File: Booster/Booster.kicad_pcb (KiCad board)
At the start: 2 copper layers, 97 x 60 mm, 120 parts, among them IC401 SN754410, J101 Track, J301 15VDC, J601 StatusLED, J701 Conn_01x04, P201 CONN_01X02, P202 CONN_01X02, P601 ~OVERCURRENT_OUT, P602 ~OVERCURRENT_OUT_OP, P603 MSTR_SW, P604 MSTR_SW_OUT, P605 MSTR_SW_OUT_OP, P606 ~DRIVER_ENABLE_OUT_OP, P607 ~DRIVER_ENABLE_OUT, P701 REVERSER_OUT, P702 REVERSER_OUT_OP, Q601 BC807-40, Q602 BC807-40, Q603 BC807-40, Q604 BC817-40, Q701 BC817-40, SW601 DIP, U201 6N137, U203 LM339, U301 LM7805_TO220, U501 LM338, U502 LM358, U503 NE555, U504 74HC08, U602 PC817, U603 PC817, U604 PC817, U701 74HC86, U702 PC817

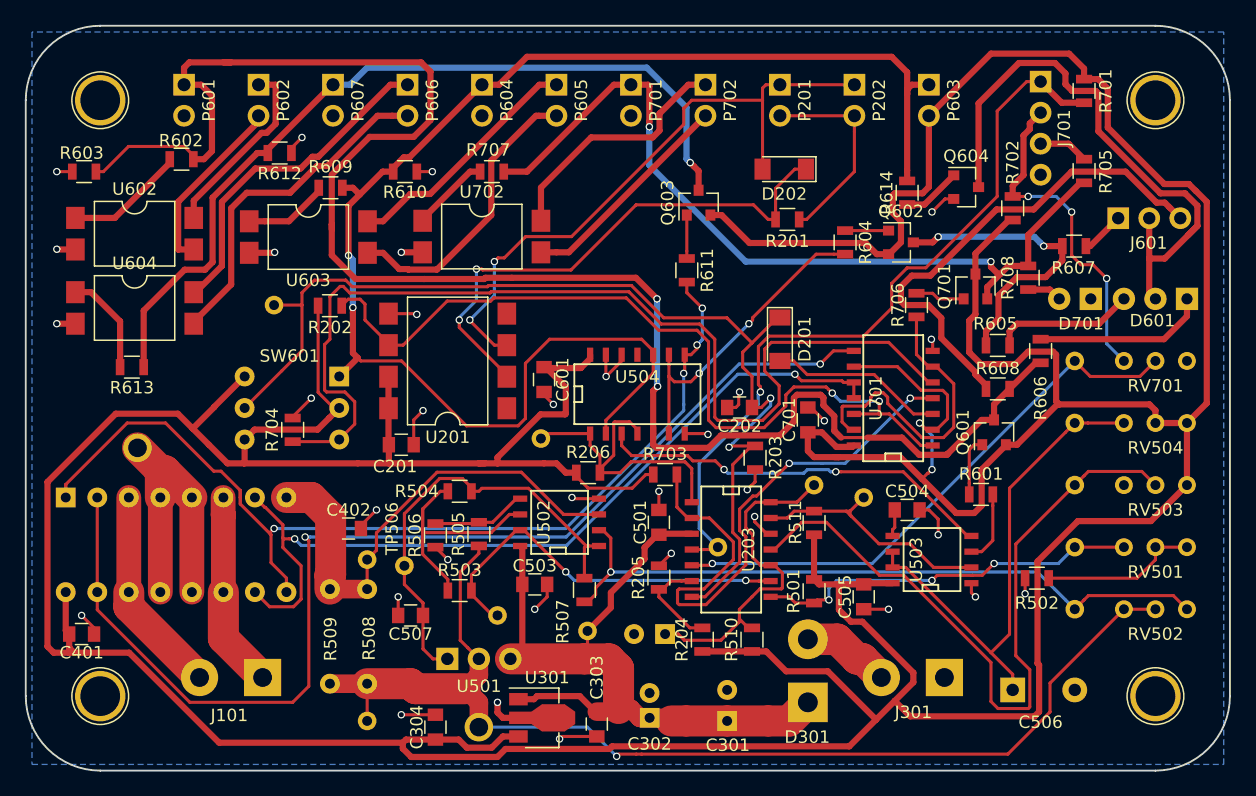
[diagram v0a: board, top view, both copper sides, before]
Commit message: Fixed track clearance (one DRC validation fail as well as a few tracks unnecessary close to through whole components.
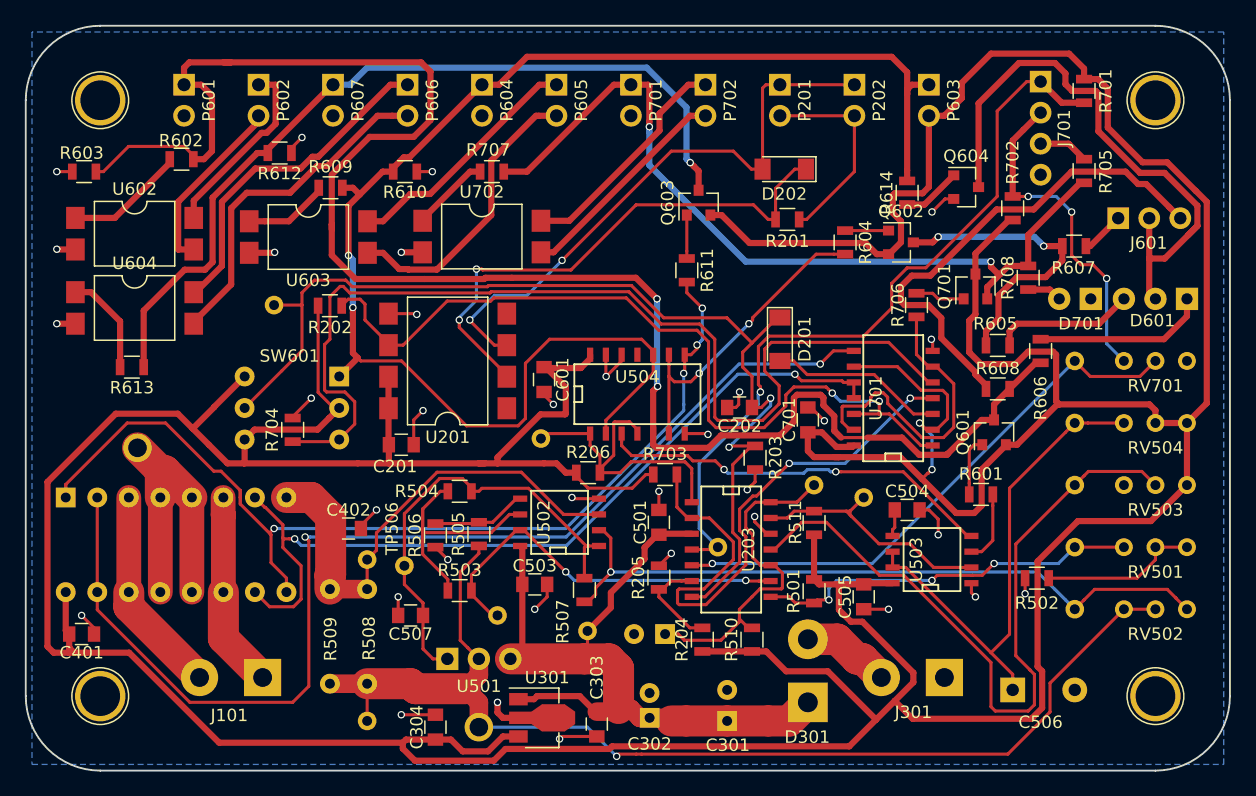
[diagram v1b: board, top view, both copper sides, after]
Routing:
- net /DCC Input/DCC_Input: track 51.2 -> 47.7 mm
- net Net-(P702-Pad1): track 20.2 -> 18.6 mm
- net +5V: track 459.4 -> 460.9 mm
- net Net-(RV503-Pad2): track 57.6 -> 58.4 mm

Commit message: Starting to add description text to connectors.
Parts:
- moved TP201 2.06 mm to (120.5, 104.5)
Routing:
- net GND: track 96.7 -> 97.8 mm
- net +5V: track 460.9 -> 461.5 mm
- net Net-(C202-Pad1): track 86.0 -> 85.5 mm
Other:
- board text added: "DCC IN"
- board text added: "DCC OUT"
- board text added: "MASTER SWITCH"
- board text added: "MASTER SWITCH OC OUT"
- board text added: "MSTR SW OUT"
- board text added: "REVERSER OC OUT"
- board text added: "REVERSER OUT"
- board text added: "~OUTPUT ENABLED OC OUT"
- board text added: "~OUTPUT ENABLED OUT"
- board text added: "~SHORT OC OUT"
- board text added: "~SHORT OUT"

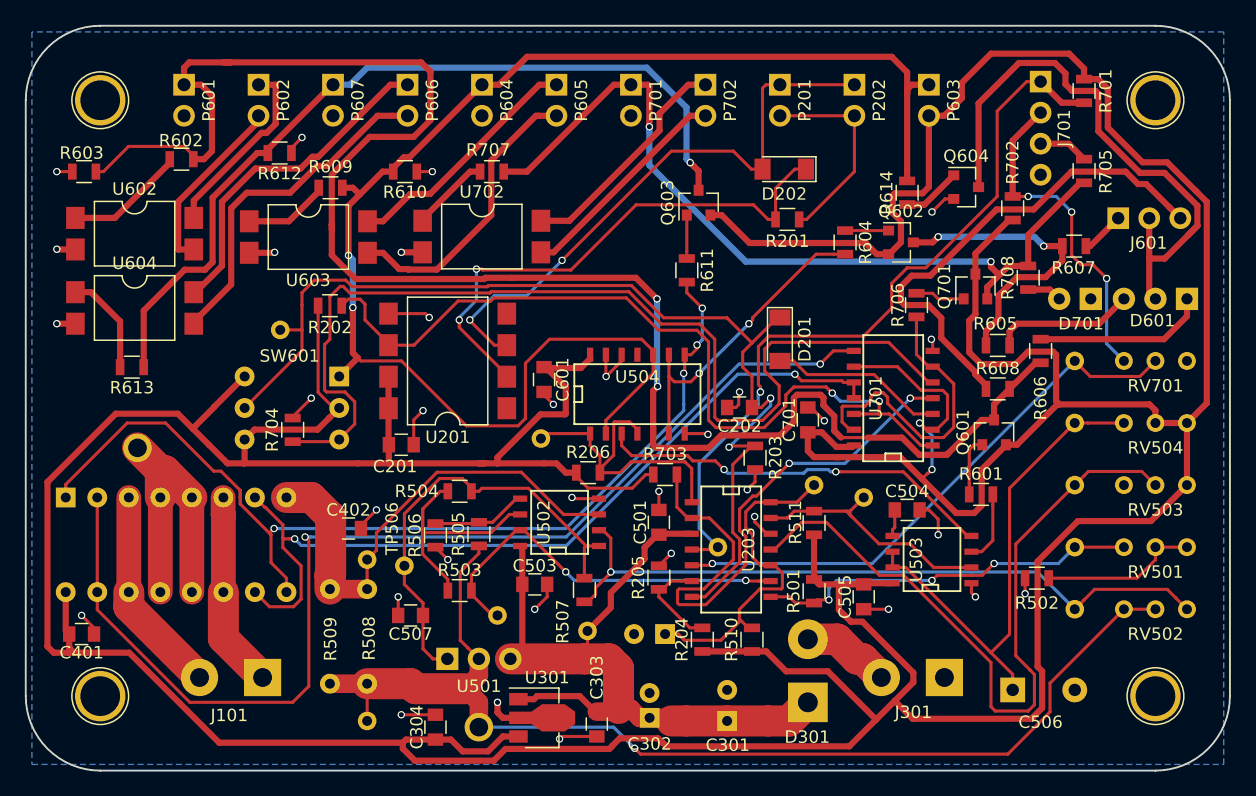
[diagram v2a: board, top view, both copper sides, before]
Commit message: Misc adjustments. Added text to all connectors.
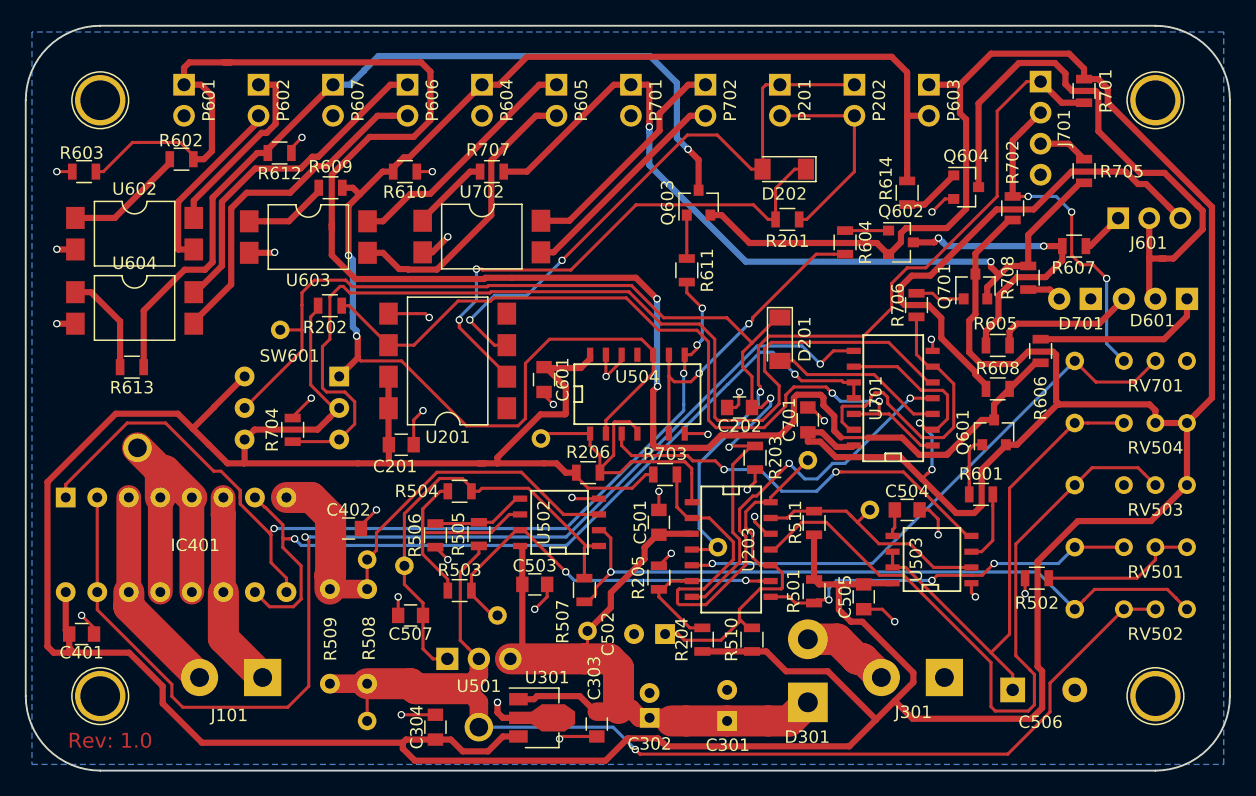
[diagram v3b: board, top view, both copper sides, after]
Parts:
- moved TP508 2.06 mm to (163.0, 115.0)
- moved TP509 1.12 mm to (168.0, 119.0)
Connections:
- P603 pad 1: /Overcurrent Detector/MSTR_SW -> +5V
- P603 pad 2: +5V -> /Overcurrent Detector/MSTR_SW
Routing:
- net Net-(IC401-Pad15): track 92.3 -> 94.4 mm
- net GND: track 97.8 -> 99.6 mm
- net +5V: track 461.5 -> 463.1 mm
- net Net-(P607-Pad1): track 69.4 -> 70.8 mm
- net /Driver/DRIVER_SIGNAL: track 67.7 -> 69.2 mm
- net /DCC Input/DCC: track 66.9 -> 65.6 mm
- net /DCC Input/DCC_Input: track 47.7 -> 48.8 mm
- net Net-(U503-Pad4): track 32.4 -> 33.4 mm
- net Net-(R703-Pad2): track 47.8 -> 48.8 mm
- net Net-(R511-Pad1): track 20.6 -> 19.8 mm
- net Net-(C502-Pad1): track 27.9 -> 28.5 mm
- net /Overcurrent Detector/MSTR_SW: track 118.5 -> 118.0 mm
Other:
- board text added: "+"
- board text added: "-"
- board text added: "DCC in"
- board text added: "DCC out"
- board text added: "Gr"
- board text added: "IR"
- board text added: "LED"
- board text added: "Master switch"
- board text added: "Master switch out"
- board text added: "Master switch out OC"
- board text added: "Maximum current"
- board text added: "Overcurrent detect delay"
- board text added: "Overcurrent release delay"
- board text added: "Overcurrent sense adjust"
- board text added: "Photo Res."
- board text added: "Red"
- board text added: "Rev: 1.0"
- board text added: "Reverser in/out"
- board text added: "Reverser out"
- board text added: "Reverser out OC"
- board text added: "Reverser sensitivity"
- board text added: "Status LED"
- board text added: "~Overcurrent out"
- board text added: "~Overcurrent out OC"
- board text added: "~Track enabled out"
- board text added: "~Track enabled out OC"
- board text removed: "DCC IN"
- board text removed: "DCC OUT"
- board text removed: "MASTER SWITCH"
- board text removed: "MASTER SWITCH OC OUT"
- board text removed: "MSTR SW OUT"
- board text removed: "REVERSER OC OUT"
- board text removed: "REVERSER OUT"
- board text removed: "~OUTPUT ENABLED OC OUT"
- board text removed: "~OUTPUT ENABLED OUT"
- board text removed: "~SHORT OC OUT"
- board text removed: "~SHORT OUT"

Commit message: Increased spacing between connectors. Various trace optimizations.
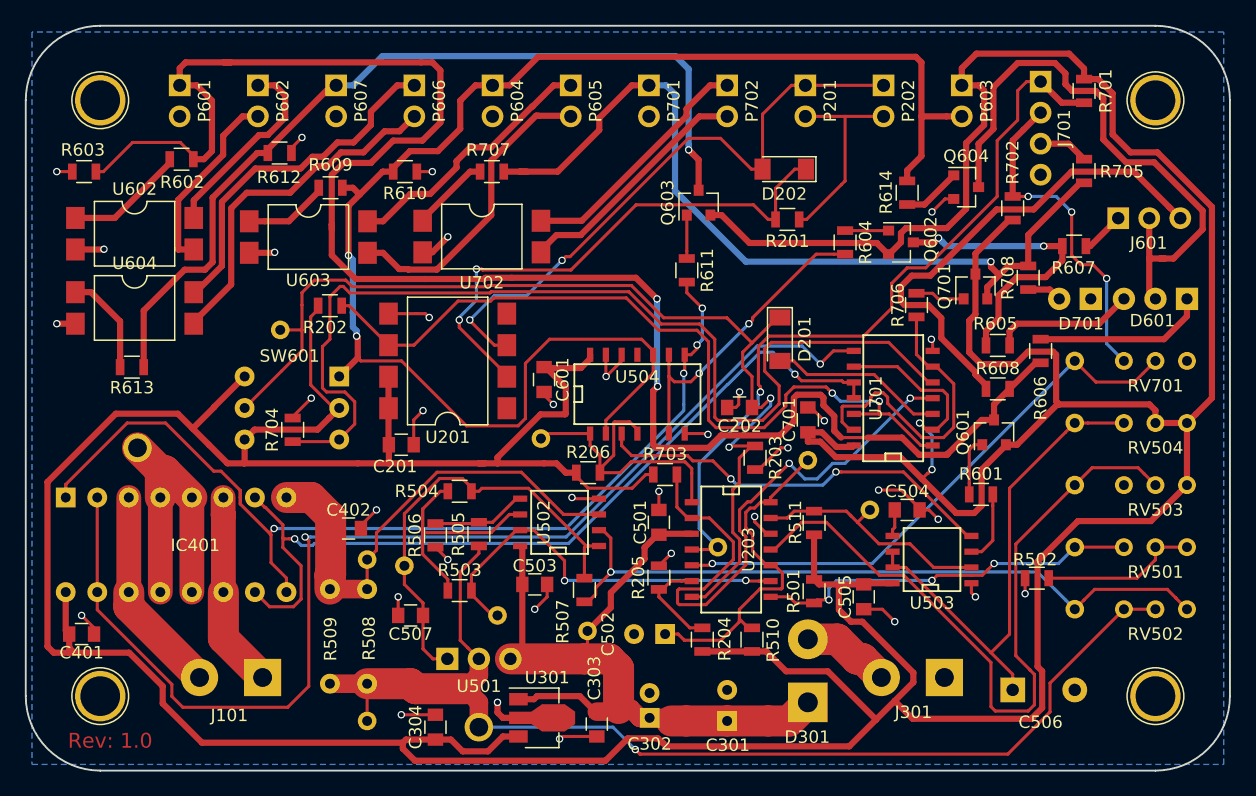
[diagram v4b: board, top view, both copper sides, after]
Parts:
- moved P603 2.65 mm to (175.4, 84.8)
- moved P202 2.35 mm to (169.1, 84.8)
- moved P201 2.05 mm to (162.8, 84.8)
- moved P702 1.75 mm to (156.5, 84.8)
- moved P701 1.45 mm to (150.2, 84.8)
- moved P605 1.15 mm to (143.9, 84.8)
- moved P604 0.85 mm to (137.6, 84.8)
- moved P606 0.55 mm to (131.3, 84.8)
- moved P601 0.35 mm to (112.4, 84.8)
- moved P607 0.25 mm to (125.0, 84.8)
- moved P602 0.07 mm to (118.7, 84.8)
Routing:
- net GND: track 99.6 -> 104.6 mm, vias 34 -> 35
- net /Overcurrent Detector/MSTR_SW: track 118.0 -> 122.9 mm
- net /Status/STATUS_GREEN_LED: track 142.4 -> 144.7 mm
- net Net-(P701-Pad1): track 66.9 -> 69.0 mm, vias 2 -> 1
- net Net-(P702-Pad2): track 17.8 -> 19.6 mm
- net Net-(P605-Pad1): track 19.8 -> 21.2 mm
- net +5V: track 463.1 -> 464.4 mm
- net Net-(R503-Pad2): track 32.0 -> 33.2 mm
- net Net-(P702-Pad1): track 18.6 -> 19.9 mm
- net Net-(P606-Pad1): track 27.2 -> 28.3 mm
- net Net-(P602-Pad2): track 14.7 -> 15.8 mm
- net /DCC Input/DCC_Input: track 48.8 -> 49.7 mm
- net Net-(P602-Pad1): track 15.1 -> 15.9 mm
- net Net-(P606-Pad2): track 27.8 -> 28.4 mm
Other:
- board text added: "Green"
- board text removed: "Gr"

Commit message: Added logos and various cleanup of traces/via positions.
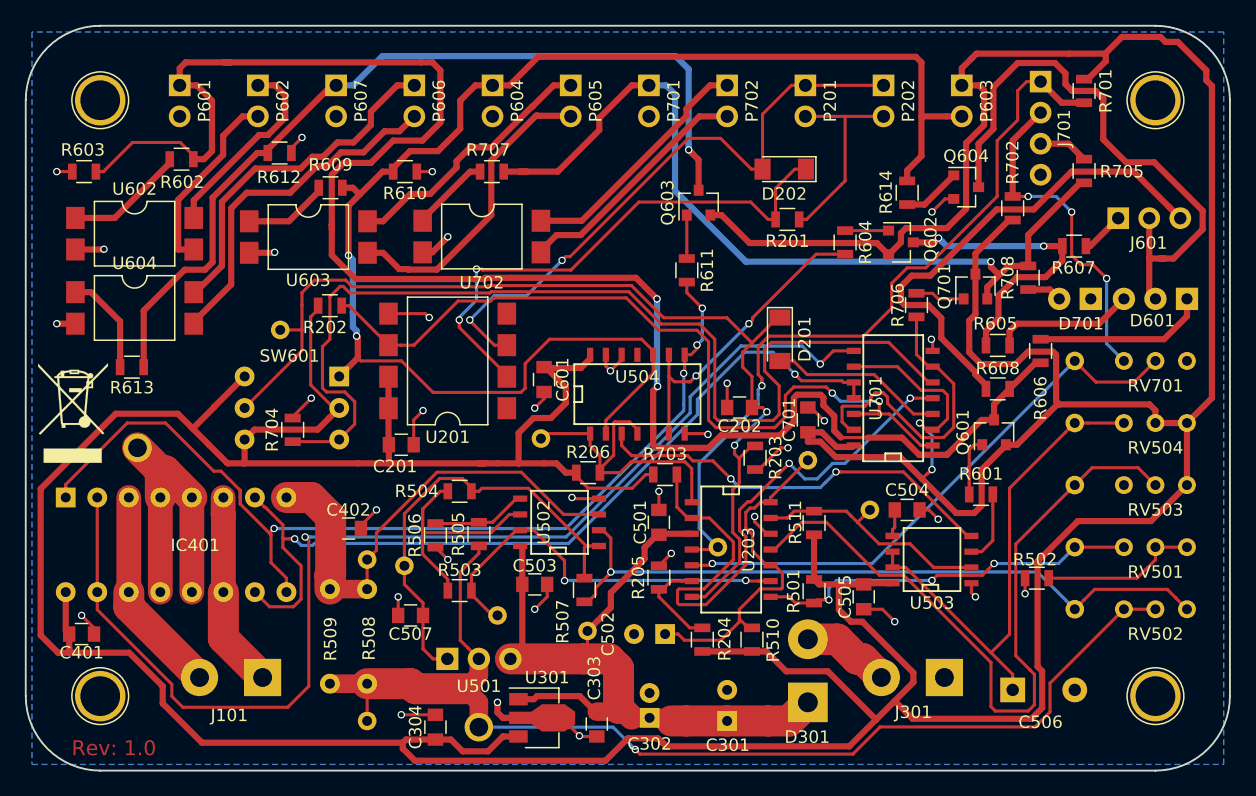
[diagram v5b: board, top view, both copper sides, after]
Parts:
- added G***: LOGO, Trainiot:TrainiotFrontMaskLogo, B.Cu at (108.9, 106.9)
- added G***: LOGO, Trainiot:TrainiotFrontMaskLogo, F.Cu at (174.9, 138.0)
- added G***: LOGO, Trainiot:BoosterSilkScreen, B.Cu at (145.8, 107.1)
- added REF***: WEEE-Logo_5.6x8mm_SilkScreen, Symbols:WEEE-Logo_5.6x8mm_SilkScreen, F.Cu at (103.8, 111.2)
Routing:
- net +5V: track 464.4 -> 471.0 mm
- net GND: track 104.6 -> 100.9 mm, vias 35 -> 34
- net /Overcurrent Detector/MSTR_SW: track 122.9 -> 119.2 mm
- net Net-(C202-Pad1): track 85.5 -> 82.6 mm
- net Net-(IC401-Pad15): track 94.4 -> 95.6 mm
- net +15V: track 62.2 -> 63.1 mm
- net /Driver/DRIVER_SIGNAL: track 69.2 -> 69.9 mm
- net Net-(R704-Pad1): track 83.3 -> 83.8 mm
- net /DCC Input/DCC: track 65.6 -> 66.1 mm

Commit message: Minor adjustment
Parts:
- moved U203 4.08 mm to (161.0, 122.7)
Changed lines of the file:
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@@
   )
   (module SMD_Packages:SOIC-14_N (layer F.Cu)
-    (at 156.952 122.19 270)
+    (at 161.002 122.71 270)
     (descr "Module CMS SOJ 14 pins Large")
     (tags "CMS SOJ")

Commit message: Turns out last minor adjustment was actually an error. :)
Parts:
- moved U203 4.08 mm to (157.0, 122.2)
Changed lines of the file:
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@@
   )
   (module SMD_Packages:SOIC-14_N (layer F.Cu)
-    (at 161.002 122.71 270)
+    (at 156.952 122.19 270)
     (descr "Module CMS SOJ 14 pins Large")
     (tags "CMS SOJ")
